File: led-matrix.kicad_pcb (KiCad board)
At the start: 2 copper layers, 91 parts, among them J1 Conn_01x01_Pin, J10 Conn_01x01_Pin, J11 Conn_01x01_Pin, J12 Conn_01x01_Pin, J13 Conn_01x01_Pin, J14 Conn_01x01_Pin, J15 Conn_01x01_Pin, J16 Conn_01x01_Pin, J17 Conn_01x01_Pin, J18 Conn_01x01_Pin, J19 Conn_01x01_Pin, J2 Conn_01x01_Pin, J20 Conn_01x01_Pin, J21 Conn_01x01_Pin, J22 Conn_01x01_Pin, J23 Conn_01x01_Pin, J3 Conn_01x01_Pin, J4 Conn_01x01_Pin, J5 Conn_01x01_Pin, J6 Conn_01x01_Pin, J7 Conn_01x01_Pin, J8 Conn_01x01_Pin, J9 Conn_01x01_Pin, U1 MAX7219, U2 Pico

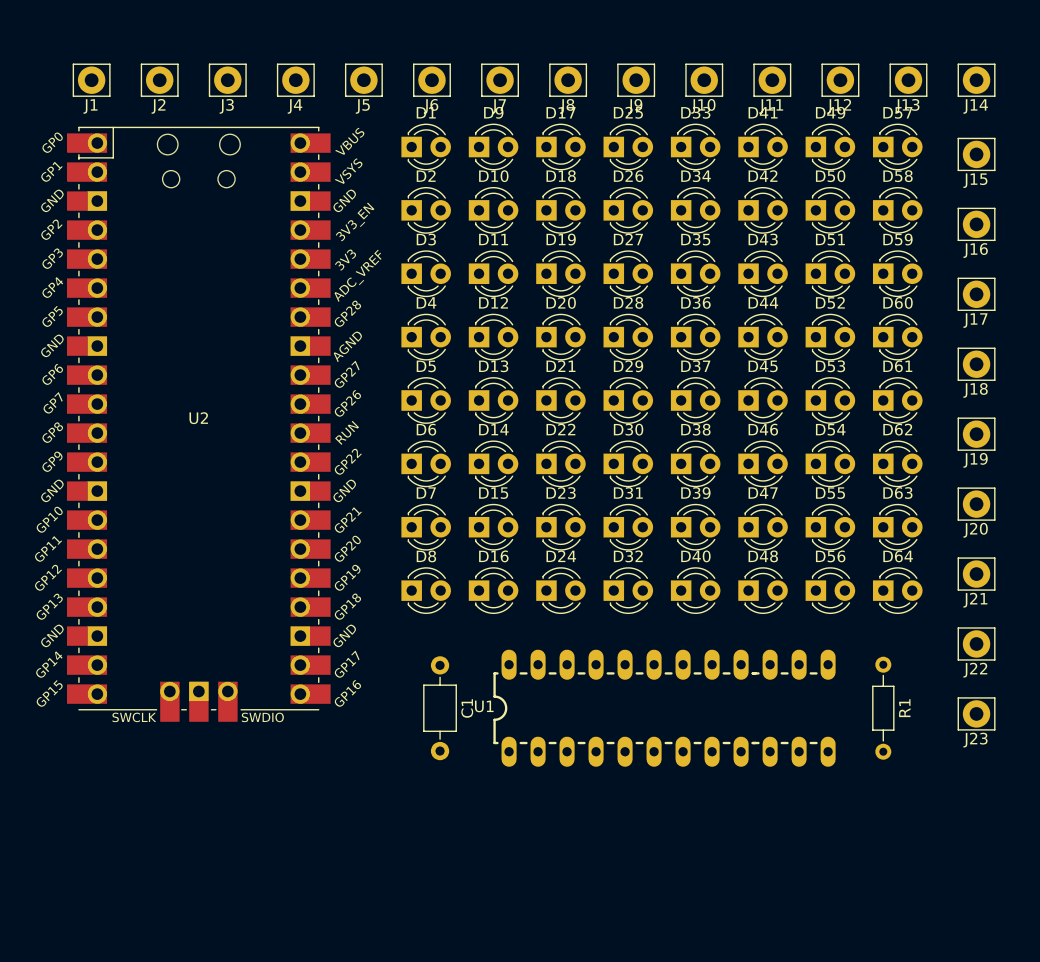
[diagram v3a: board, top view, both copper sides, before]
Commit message: chore: remove silkscreen layers for the leds and gpios
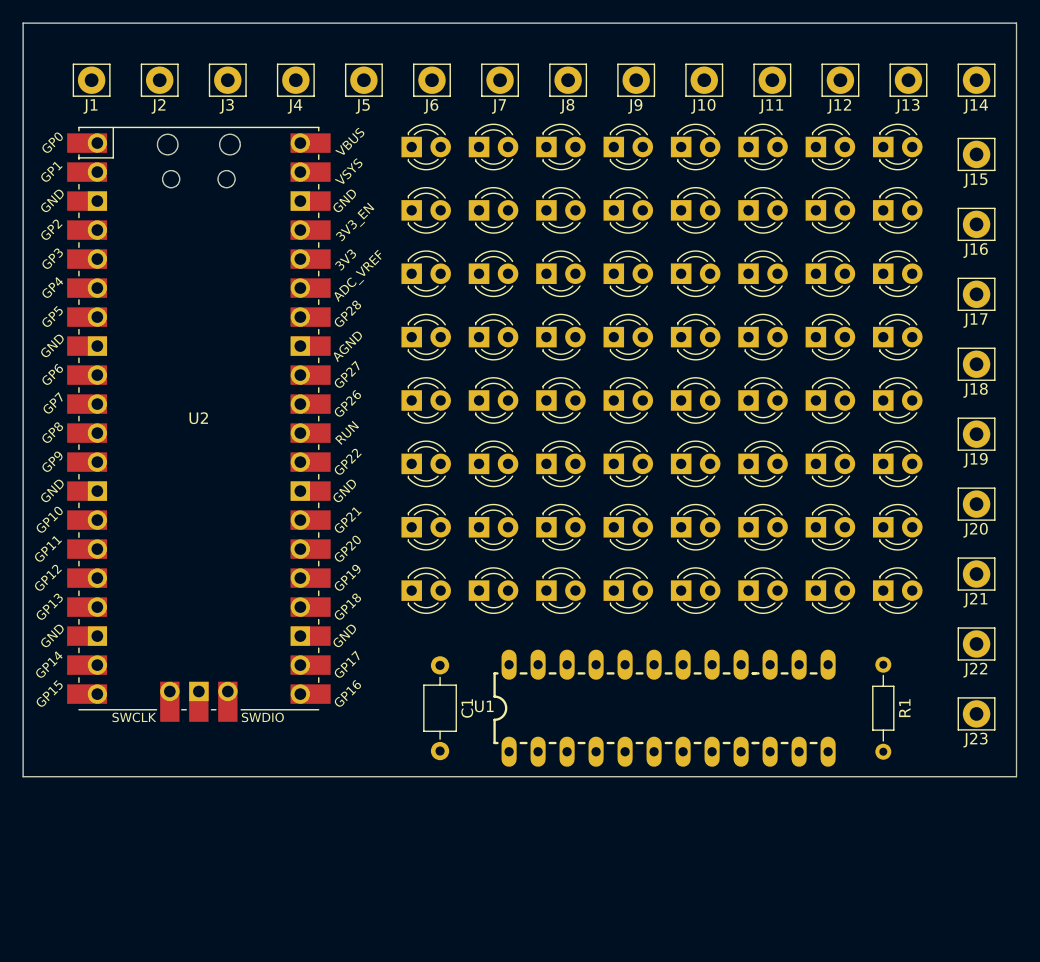
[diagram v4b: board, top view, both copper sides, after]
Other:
- board outline added: 87 x 66 mm

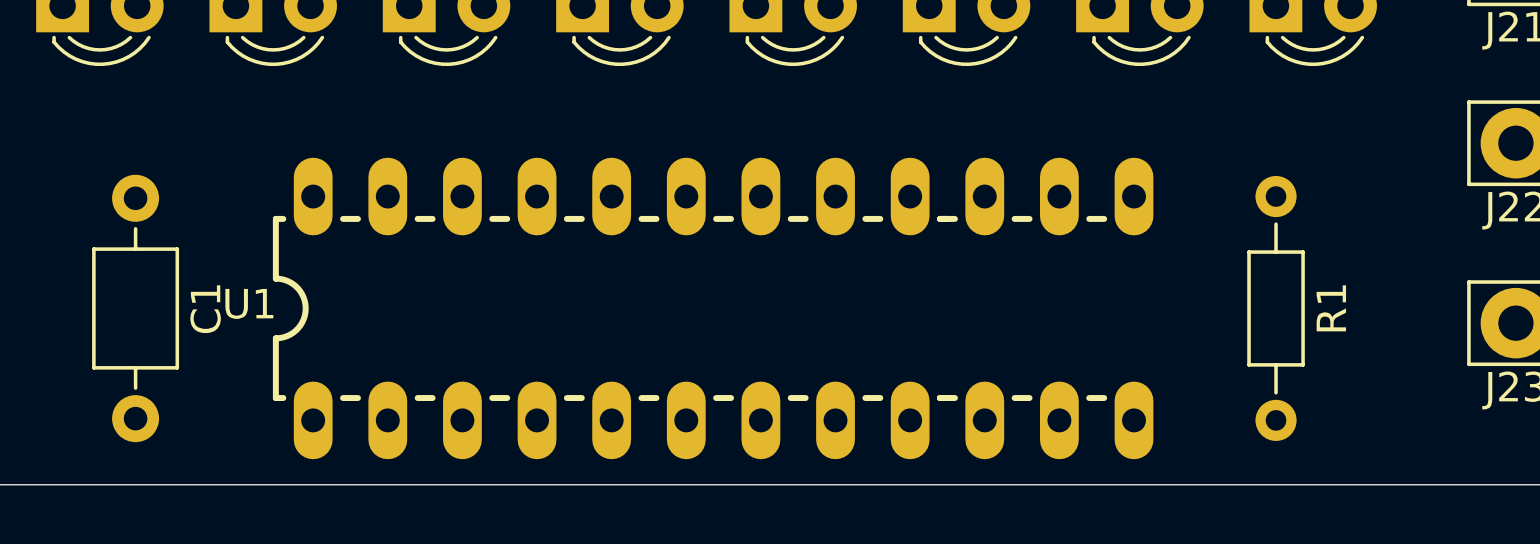
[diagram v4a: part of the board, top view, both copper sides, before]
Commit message: chore: remove redundant grounds from gpio
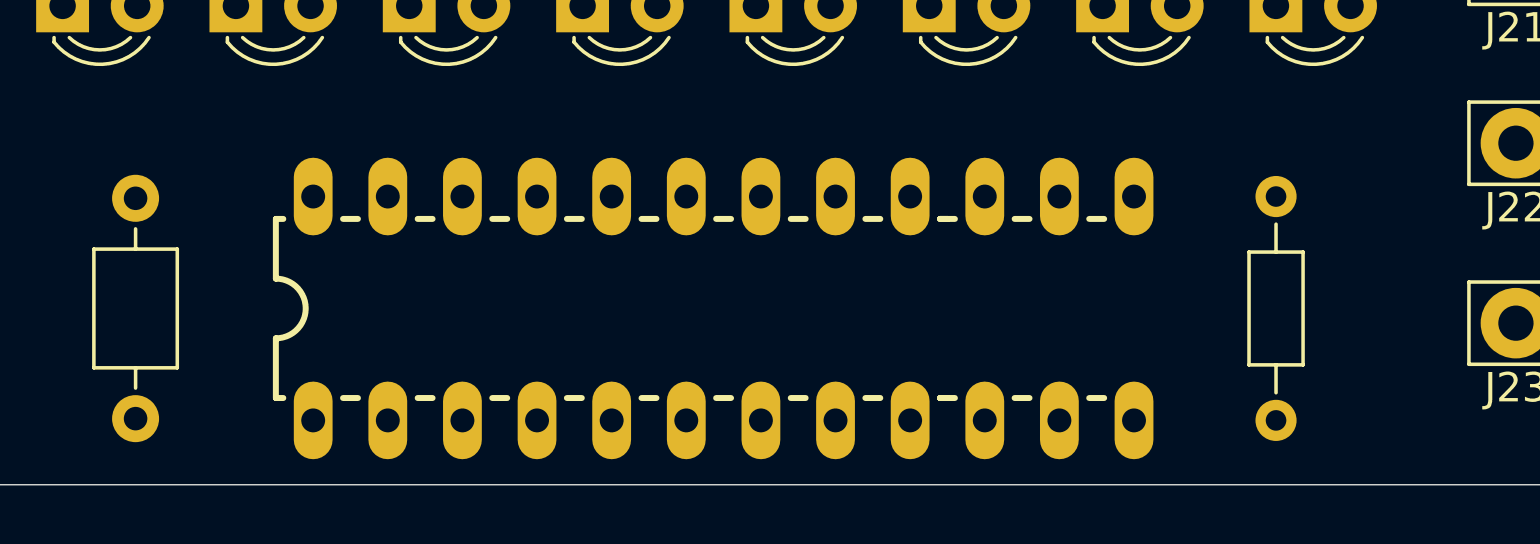
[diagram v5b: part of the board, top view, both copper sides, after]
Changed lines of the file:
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@@
 			(at 3.81 -1.92 -90)
 			(layer "F.SilkS")
+			(hide yes)
 			(effects
 				(font
@@
 			(at 3.75 -2.42 90)
 			(layer "F.SilkS")
+			(hide yes)
 			(effects
 				(font
@@
 			(at -16.137745 -0.127075 180)
 			(layer "F.SilkS")
+			(hide yes)
 			(effects
 				(font

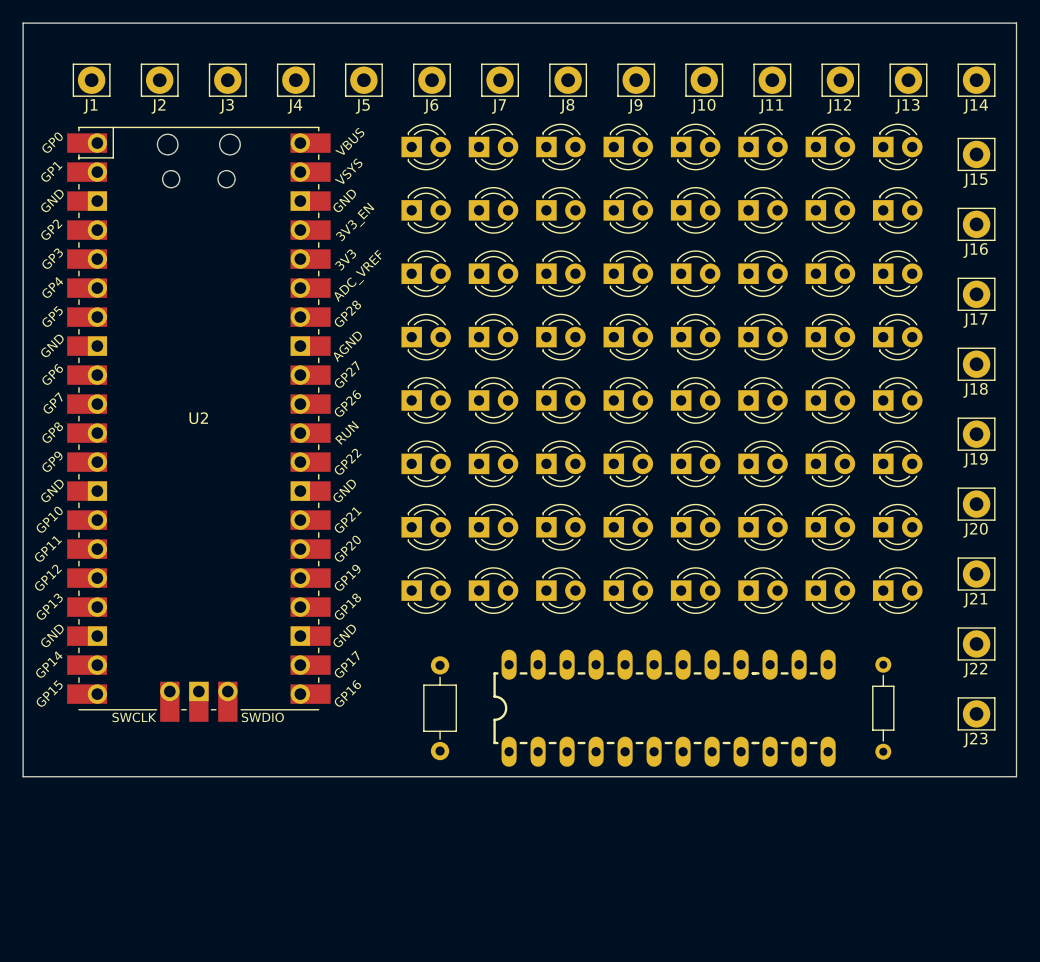
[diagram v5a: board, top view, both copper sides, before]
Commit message: feat: change gpio names and move positions on pcb
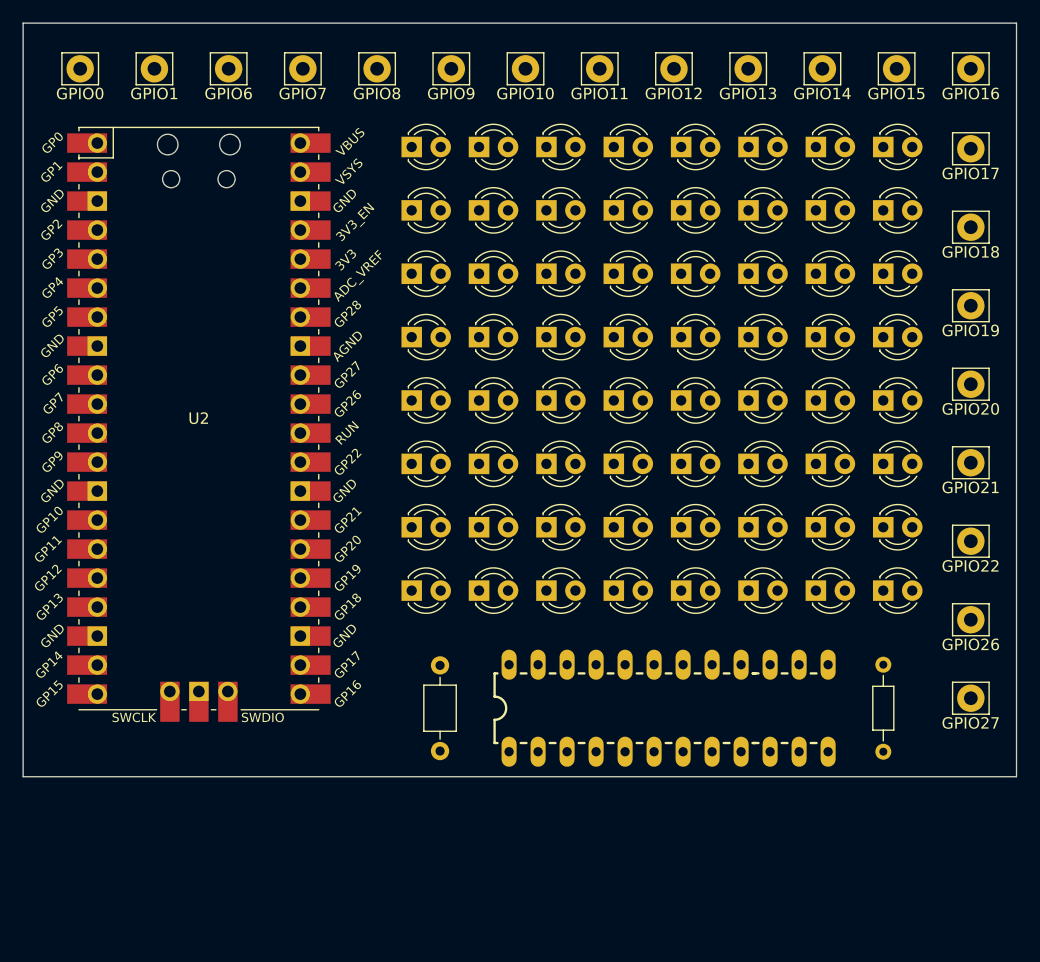
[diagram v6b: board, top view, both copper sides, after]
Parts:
- removed J22, J23: Conn_01x01_Pin, Connector_Pin:Pin_D1.2mm_L11.3mm_W3.0mm_Flat
- moved GPIO9 31.5 mm to (127.5, 64.0)
- moved GPIO1 24.3 mm to (101.5, 64.0)
- moved GPIO8 13.1 mm to (121.0, 64.0)
- moved GPIO6 11.9 mm to (108.0, 64.0)
- moved GPIO27 10.9 mm to (173.0, 119.1)
- moved GPIO26 10.1 mm to (173.0, 112.2)
- moved GPIO22 9.39 mm to (173.0, 105.4)
- moved GPIO21 8.64 mm to (173.0, 98.5)
- moved GPIO20 7.89 mm to (173.0, 91.6)
- moved GPIO19 7.14 mm to (173.0, 84.8)
- moved GPIO0 7.03 mm to (95.0, 64.0)
- moved GPIO18 6.39 mm to (173.0, 77.9)
- moved GPIO17 6.02 mm to (173.0, 71.0)
- moved GPIO16 5.55 mm to (173.0, 64.0)
- moved GPIO15 5.02 mm to (166.5, 64.0)
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- renumbered J2 to GPIO0, J6 to GPIO1, J7 to GPIO10, J8 to GPIO11, J9 to GPIO12, J10 to GPIO13, J11 to GPIO14, J12 to GPIO15, J13 to GPIO16, J14 to GPIO17, J15 to GPIO18, J16 to GPIO19, J17 to GPIO20, J18 to GPIO21, J19 to GPIO22, J20 to GPIO26, J21 to GPIO27, J5 to GPIO6, J4 to GPIO7, J3 to GPIO8, J1 to GPIO9
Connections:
- GPIO18 pad 1: Net-(J15-Pin_1) -> Net-(GPIO18-Pin_1)
- GPIO19 pad 1: Net-(J16-Pin_1) -> Net-(GPIO19-Pin_1)
- GPIO20 pad 1: Net-(J17-Pin_1) -> Net-(GPIO20-Pin_1)
- GPIO21 pad 1: Net-(J18-Pin_1) -> Net-(GPIO21-Pin_1)
- GPIO22 pad 1: Net-(J19-Pin_1) -> Net-(GPIO22-Pin_1)
- GPIO26 pad 1: Net-(J20-Pin_1) -> Net-(GPIO26-Pin_1)
- GPIO27 pad 1: Net-(J21-Pin_1) -> Net-(GPIO27-Pin_1)
- U1 pad 4: Net-(C1-Pad2) -> Net-(U1-GND-Pad4)
- U1 pad 9: Net-(C1-Pad2) -> Net-(U1-GND-Pad4)
- U2 pad 23: Net-(J15-Pin_1) -> Net-(C1-Pad2)
- U2 pad 24: Net-(J16-Pin_1) -> Net-(GPIO18-Pin_1)
- U2 pad 25: Net-(J17-Pin_1) -> Net-(GPIO19-Pin_1)
- U2 pad 26: Net-(J18-Pin_1) -> Net-(GPIO20-Pin_1)
- U2 pad 27: Net-(J19-Pin_1) -> Net-(GPIO21-Pin_1)
- U2 pad 28: Net-(J20-Pin_1) -> unconnected-(U2-GND-Pad28)
- U2 pad 29: Net-(J21-Pin_1) -> Net-(GPIO22-Pin_1)
- U2 pad 31: Net-(J22-Pin_1) -> Net-(GPIO26-Pin_1)
- U2 pad 32: Net-(J23-Pin_1) -> Net-(GPIO27-Pin_1)
- U2 pad 38: Net-(C1-Pad2) -> Net-(U1-GND-Pad4)
